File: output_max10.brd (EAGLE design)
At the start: 73.9 x 54.2 mm, 70 parts, among them IC4 IS61WV1288EEBLL-10HLI, IC5 10M04EQFP144, Q1 25MHz

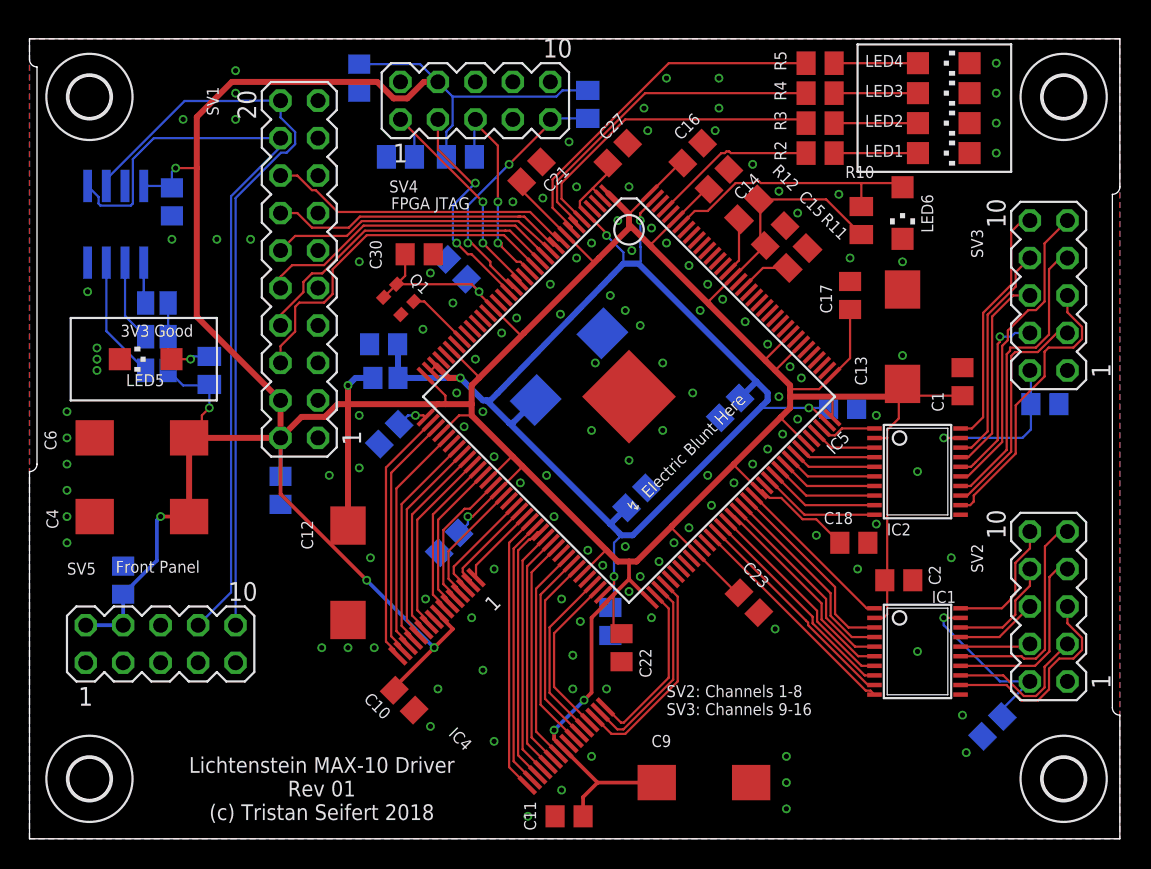
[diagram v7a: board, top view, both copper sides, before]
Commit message: Minor component placemnet changes for MAX10 output board to fix mechanical issues
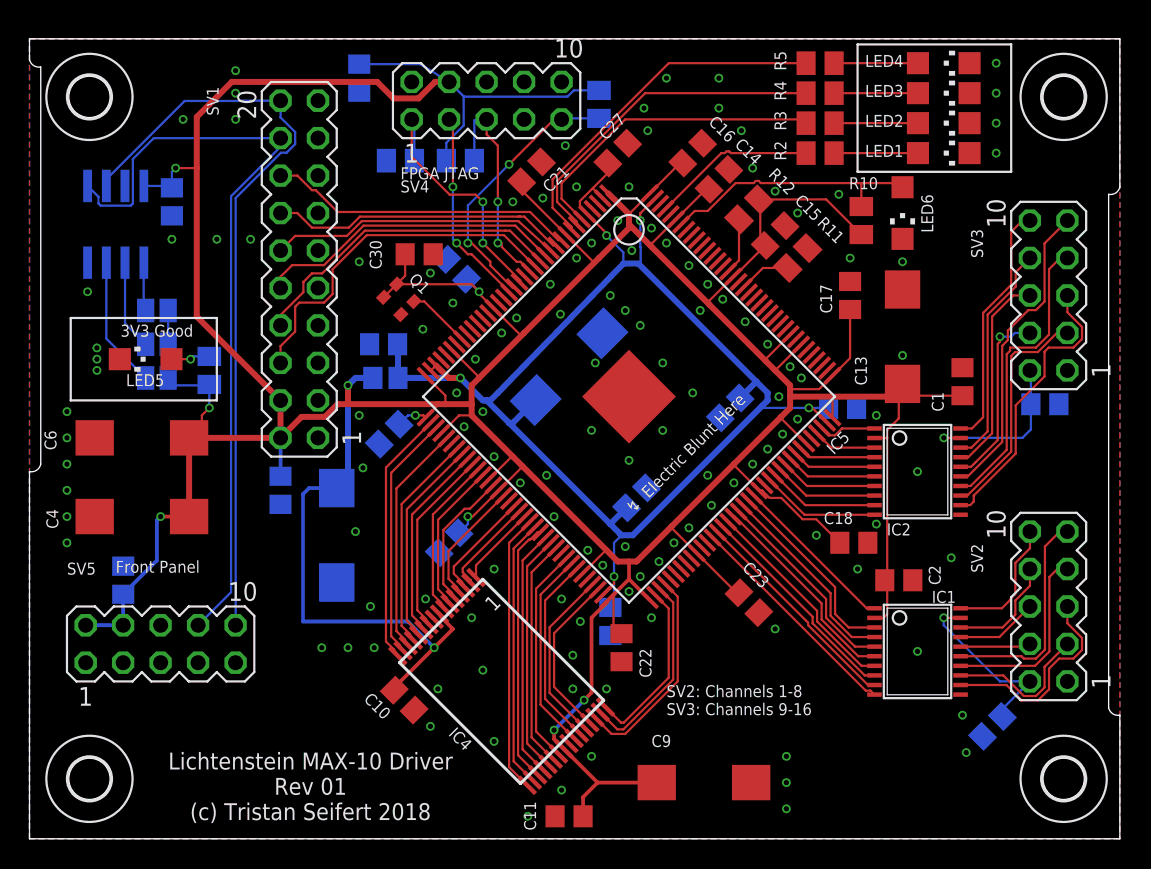
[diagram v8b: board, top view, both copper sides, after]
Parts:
- added WEED1: WEED, lichtenstein_onion:DOINK
- R10: value 10k/680R?? -> 10k
- moved C12 2.65 mm to (20.8, 20.6), flipped to the bottom
- moved R8 0.76 mm to (38.6, 49.8)
- moved SV4 0.76 mm to (31.0, 50.0)
- moved SJ2 0.51 mm to (8.64, 33.5)
- moved SJ3 0.51 mm to (8.64, 35.8)
- moved SJ1 0.51 mm to (8.64, 31.2)
- moved R7 0.25 mm to (29.2, 46.0)
- moved R9 0.25 mm to (25.1, 46.0)
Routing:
- net +3V3: track 392.6 -> 395.7 mm, vias 11 -> 10
- net JTAG_TDO: track 15.3 -> 13.6 mm
- net JTAG_TMS: track 14.7 -> 15.4 mm
- net JTAG_TCK: track 17.3 -> 18.0 mm
- net JTAG_TDI: track 17.8 -> 18.4 mm
- net N$6: track 5.60 -> 6.11 mm
- net N$5: track 8.41 -> 8.92 mm
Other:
- outline, holes or cut-outs redrawn
